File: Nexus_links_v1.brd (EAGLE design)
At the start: 19 x 99.6 mm, 42 parts, among them IC1 TL074D, IC4 TL074D, J1 PJ301_THONKICONN6, J10 PJ301_THONKICONN6, J11 PJ301_THONKICONN6, J12 PJ301_THONKICONN6, J2 PJ301_THONKICONN6, J3 PJ301_THONKICONN6, J4 PJ301_THONKICONN6, J5 PJ301_THONKICONN6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

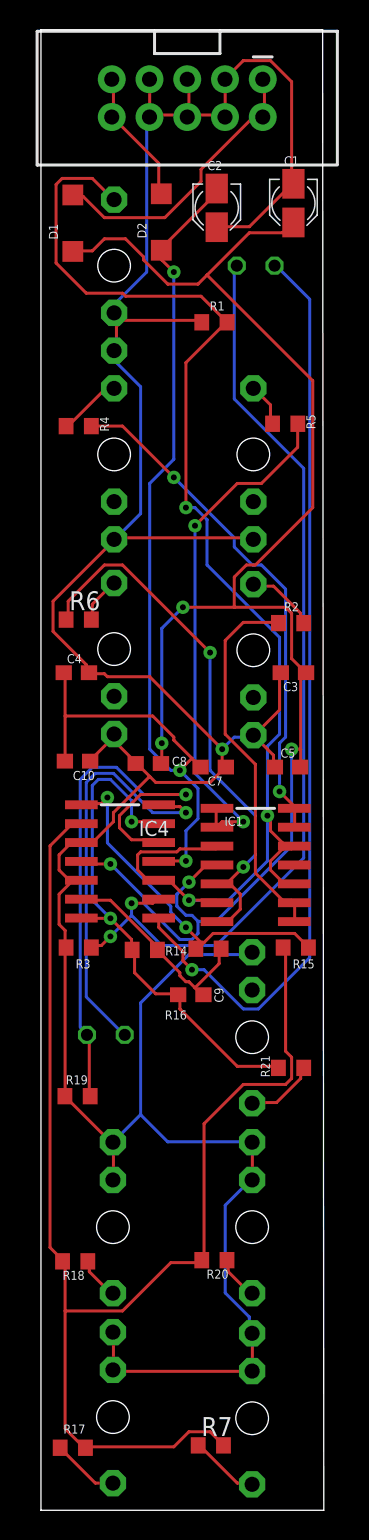
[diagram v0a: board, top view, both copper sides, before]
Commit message: Fixed power connector
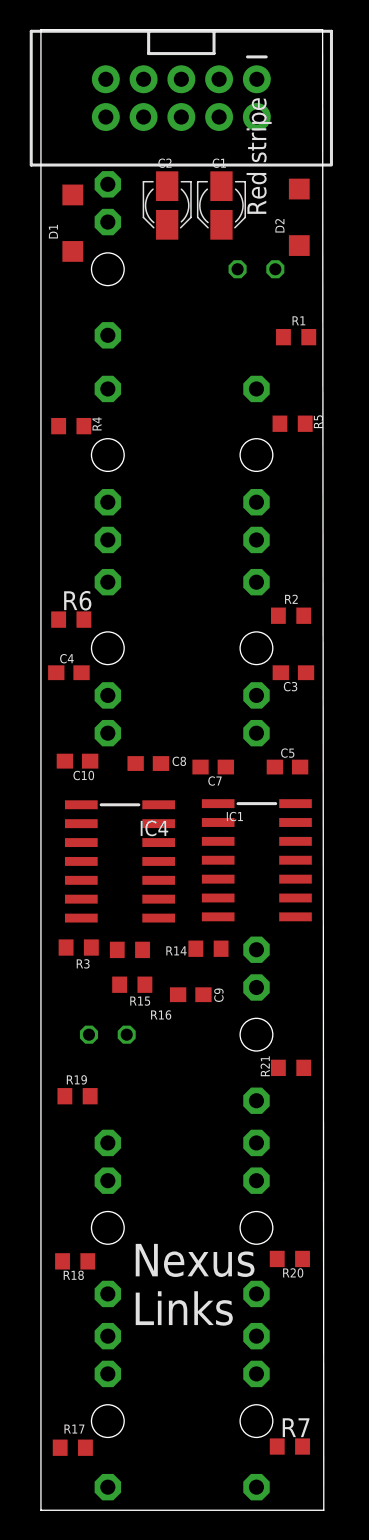
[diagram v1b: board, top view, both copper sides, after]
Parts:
- moved R15 11.3 mm to (6.14, 35.4)
- moved D2 9.29 mm to (17.4, 87.0)
- moved R1 5.59 mm to (17.2, 78.9)
- moved R7 5.32 mm to (16.7, 4.29)
- moved R20 5.08 mm to (16.7, 16.9)
- moved C1 4.84 mm to (12.1, 87.8)
- moved C2 3.34 mm to (8.49, 87.8)
- moved R16 1.00 mm to (5.99, 37.7)
- moved C4 0.50 mm to (1.88, 56.4)
- moved R2 0.50 mm to (16.8, 60.2)
- moved R4 0.50 mm to (2.04, 72.9)
- moved R5 0.50 mm to (16.9, 73.1)
- moved R6 0.50 mm to (2.04, 59.9)
- moved J1 0.49 mm to (4.50, 83.5), turned to 180 degrees
- moved J11 0.44 mm to (4.50, 6.00)
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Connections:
- net N$18: now also IC4.12; no longer IC4.13
- net N$19: now also IC4.13; no longer IC4.12
- net N$20: now also D1.A; no longer D2.C
- net N$6: now also D2.C; no longer D1.A
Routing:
- net GND: track 216.3 -> 0.00 mm, vias 1 -> 0
- net VCC: track 108.6 -> 0.00 mm, vias 5 -> 0
- net N$7: track 91.3 -> 0.00 mm, vias 3 -> 0
- net N$24: track 90.6 -> 0.00 mm
- net VEE: track 69.7 -> 0.00 mm, vias 3 -> 0
- net N$21: track 63.2 -> 0.00 mm, vias 2 -> 0
- net N$8: track 62.4 -> 0.00 mm, vias 1 -> 0
- net N$19: track 38.7 -> 0.00 mm, vias 1 -> 0
- net N$1: track 37.4 -> 0.00 mm, vias 2 -> 0
- net N$18: track 35.2 -> 0.00 mm, vias 2 -> 0
- net N$3: track 35.2 -> 0.00 mm, vias 2 -> 0
- net N$5: track 34.6 -> 0.00 mm, vias 2 -> 0
- net N$30: track 28.2 -> 0.00 mm, vias 1 -> 0
- net N$4: track 25.3 -> 0.00 mm
- net N$25: track 22.9 -> 0.00 mm, vias 2 -> 0
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
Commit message: Added ground plane
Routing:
- net GND: track 0.00 -> 216.2 mm, vias 0 -> 1
- net VEE: track 0.00 -> 96.3 mm, vias 0 -> 5
- net VCC: track 0.00 -> 92.5 mm, vias 0 -> 4
- net N$21: track 0.00 -> 85.2 mm, vias 0 -> 2
- net N$24: track 0.00 -> 84.8 mm, vias 0 -> 2
- net N$7: track 0.00 -> 82.4 mm, vias 0 -> 3
- net N$8: track 0.00 -> 54.2 mm, vias 0 -> 1
- net N$1: track 0.00 -> 39.6 mm, vias 0 -> 2
- net N$5: track 0.00 -> 35.6 mm, vias 0 -> 2
- net N$3: track 0.00 -> 33.7 mm
- net N$4: track 0.00 -> 32.1 mm, vias 0 -> 2
- net N$18: track 0.00 -> 31.8 mm, vias 0 -> 3
- net N$19: track 0.00 -> 28.4 mm, vias 0 -> 1
- net N$25: track 0.00 -> 20.7 mm, vias 0 -> 3
- net N$30: track 0.00 -> 17.9 mm, vias 0 -> 1
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- added copper zone on layer 1, net N$15
